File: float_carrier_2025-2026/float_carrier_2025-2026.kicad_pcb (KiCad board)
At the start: 2 copper layers, 86.4 x 86.4 mm, 21 parts, among them J1 Conn_01x18_Socket, J2 Conn_01x18_Socket, J3 Screw_Terminal_01x04_Depth_Se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, J4 Screw_Terminal_01x03_Servo, J5 Screw_Terminal_01x03_GND, J6 Conn_01x07_Socket, J7 Screw_Terminal_01x02, U2 TPS563200

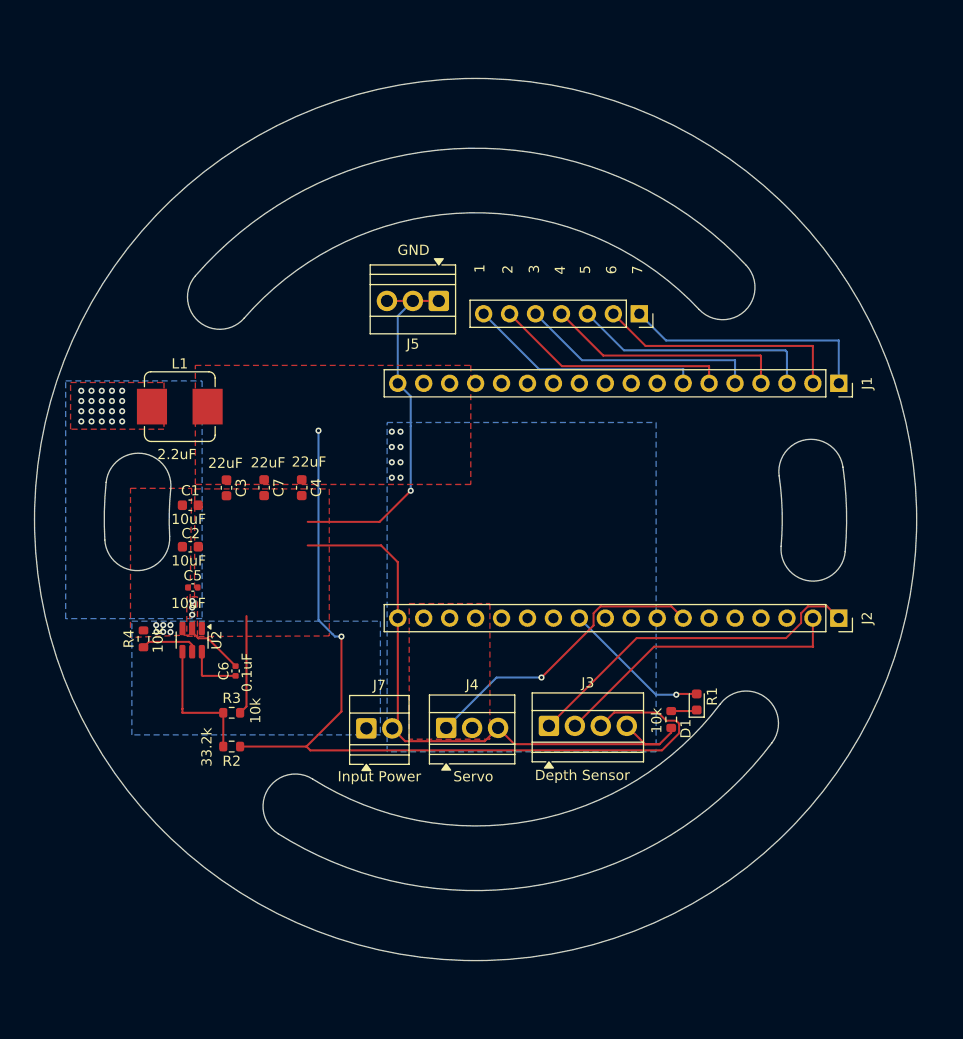
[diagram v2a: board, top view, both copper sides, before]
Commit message: Feat[float_carrier_2025-2026]
dimensions changed, hole position changed, board smaller.
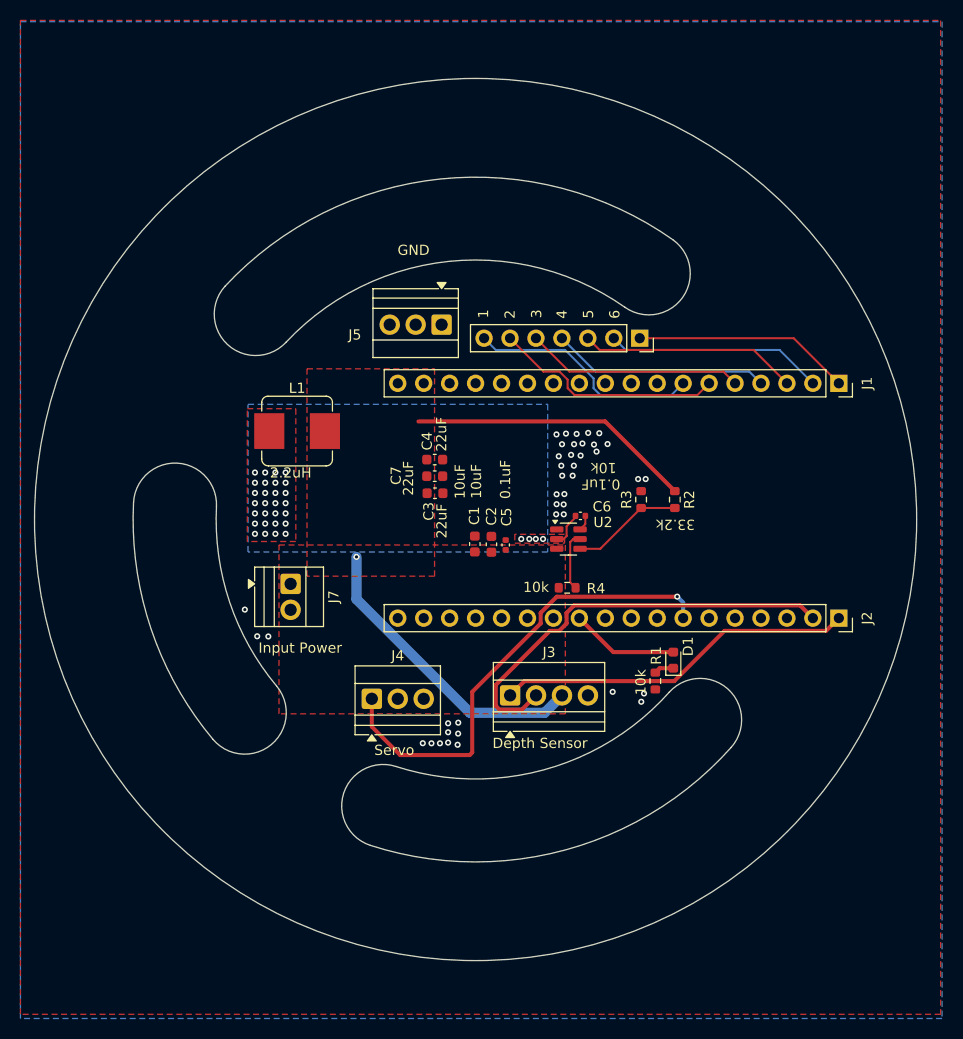
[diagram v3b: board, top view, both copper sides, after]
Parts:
- moved R2 49.7 mm to (121.1, 99.6), turned to -90 degrees
- moved R3 45.2 mm to (117.8, 99.6), turned to 90 degrees
- moved R4 41.8 mm to (110.6, 108.3), turned to 180 degrees
- moved U2 38.1 mm to (110.7, 103.5), turned to 0 degrees
- moved C6 37.0 mm to (111.9, 101.2), turned to 180 degrees
- moved C5 30.9 mm to (104.5, 104.1), turned to 90 degrees
- moved C2 29.5 mm to (103.1, 104.0), turned to 90 degrees
- moved C1 28.1 mm to (101.5, 104.0), turned to 90 degrees
- moved C3 20.4 mm to (97.6, 99.0), turned to 0 degrees
- moved C7 16.7 mm to (97.6, 97.4), turned to 0 degrees
- moved J7 16.0 mm to (83.5, 107.9), turned to -90 degrees
- moved C4 13.3 mm to (97.6, 95.7), turned to 0 degrees
- moved L1 11.7 mm to (84.1, 92.9)
- moved J4 7.82 mm to (91.4, 119.2)
- moved J3 4.83 mm to (105.0, 118.8)
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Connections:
- J4 pad 2: /5V -> /6V
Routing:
- net GND: track 106.3 -> 0.28 mm, vias 1 -> 41
- net /3.3V: track 87.1 -> 57.5 mm, vias 10 -> 1
- net /GPIO33: track 29.3 -> 46.6 mm
- net /GPIO20/SCA: track 29.3 -> 42.1 mm
- net Net-(U2-VBST): track 5.63 -> 1.54 mm
- net /GPIO0: track 14.6 -> 10.6 mm, vias 1 -> 0
- net /GPIO7: track 24.8 -> 21.3 mm
- net /GPIO6: track 24.5 -> 21.3 mm
- net /GPIO5: track 24.2 -> 21.3 mm
- net /GPIO4: track 23.9 -> 21.3 mm
- net Net-(U2-SW): track 6.72 -> 4.16 mm, vias 23 -> 32
- net /GPIO3: track 23.7 -> 21.3 mm
- net Net-(U2-VFB): track 13.3 -> 10.9 mm
- net /GPIO19/SCL: track 34.3 -> 35.3 mm
- net Net-(D1-K): track 2.54 -> 1.94 mm
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- added copper zone on B.Cu, net GND
- removed copper zone on B.Cu, net /3.3V
- removed copper zone on F.Cu, net /5V
- removed copper zone on B.Cu, net /6V
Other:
- outline, holes or cut-outs redrawn
- board text added: "2.2uH"
- board text removed: "2.2uF"
- board text removed: "7"
